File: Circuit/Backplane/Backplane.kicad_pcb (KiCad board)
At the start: 2 copper layers, 90.2 x 288.5 mm, 86 parts, among them CON1 peripheral_bridge, CON2 power_distributor, J1 USB_OTG, J2 power_source_mode, J3 general_power_source, J4 pneumatic, J5 pressure_sensor, J6 RS232_DVL, P1 imaging_sonar, P2 DVL, P3 computer1, P4 computer2, P5 ethernet_switch, P6 general, Q1 BC817-40, U1 LM1117-3.3, U2 TUSB4041I, U3 TLV73311PDBVT, Y1 24MHz

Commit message: FixVpcieWire
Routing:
- net VPCIE: track 224.6 -> 277.8 mm, vias 10 -> 11
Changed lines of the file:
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@@
   (general
     (links 258)
-    (no_connects 67)
-    (area 54.888001 -28.941011 180.062 277.020001)
+    (no_connects 2)
+    (area 76.124999 -26.745001 166.445001 261.949001)
     (thickness 1.6)
-    (drawings 32)
-    (tracks 1596)
+    (drawings 34)
+    (tracks 1606)
     (zones 0)
     (modules 86)
@@
   )
   (setup
-    (last_trace_width 0.254)
+    (last_trace_width 0.3048)
     (user_trace_width 0.2794)
     (user_trace_width 0.3048)
@@
     )
   )
+  (gr_line (start 134.62 160.02) (end 134.62 -7.62) (layer F.SilkS) (width 0.2))
+  (gr_line (start 91.44 119.888) (end 91.44 260.096) (layer F.SilkS) (width 0.2))
   (dimension 139.7 (width 0.3) (layer Eco1.User)
     (gr_text "139.700 mm" (at 124.126 62.268443 270) (layer Eco1.User)
@@
     (arrow2b (pts (xy 85.09 -25.4) (xy 85.676421 -24.273496)))
   )
-  (gr_text DSP (at 82.55 198.12 90) (layer Eco2.User)
+  (gr_text DSP (at 85.598 177.546 90) (layer Eco2.User)
     (effects (font (size 1.5 1.5) (thickness 0.3)))
   )
@@
     (arrow2b (pts (xy 91.44 119.634) (xy 90.853579 118.507496)))
   )
+  (segment (start 164.592 71.48373) (end 164.592 57.8612) (width 0.3048) (layer B.Cu) (net 1))
+  (segment (start 164.592 57.8612) (end 160.782 54.0512) (width 0.3048) (layer B.Cu) (net 1))
+  (segment (start 157.988 100.838) (end 159.283399 99.542601) (width 0.3048) (layer B.Cu) (net 1))
+  (segment (start 159.283399 99.542601) (end 159.283399 76.792331) (width 0.3048) (layer B.Cu) (net 1))
+  (segment (start 159.283399 76.792331) (end 164.592 71.48373) (width 0.3048) (layer B.Cu) (net 1))
+  (segment (start 159.512 102.108) (end 161.798 102.108) (width 0.3048) (layer F.Cu) (net 1))
+  (segment (start 157.988 102.108) (end 159.512 102.108) (width 0.3048) (layer F.Cu) (net 1))
+  (segment (start 159.512 102.108) (end 159.258 102.108) (width 0.3048) (layer F.Cu) (net 1))
+  (segment (start 159.258 102.108) (end 157.988 100.838) (width 0.3048) (layer F.Cu) (net 1))
+  (via (at 157.988 100.838) (size 1.10236) (drill 0.6096) (layers F.Cu B.Cu) (net 1))
   (segment (start 156.21 103.886) (end 157.988 102.108) (width 0.3048) (layer F.Cu) (net 1))
-  (segment (start 157.988 102.108) (end 161.798 102.108) (width 0.3048) (layer F.Cu) (net 1))
   (segment (start 149.352 108.204) (end 153.67 103.886) (width 0.3048) (layer B.Cu) (net 1))
   (segment (start 153.67 103.886) (end 156.21 103.886) (width 0.3048) (layer B.Cu) (net 1))
@@
   (segment (start 156.445799 -21.192201) (end 157.226 -20.412) (width 0.254) (layer F.Cu) (net 140))
   (segment (start 157.226 -20.412) (end 157.226 -19.558) (width 0.254) (layer F.Cu) (net 140))
+  (segment (start 143.885919 79.502) (end 143.885919 42.804081) (width 0.2794) (layer F.Cu) (net 141))
+  (segment (start 144.18309 83.096347) (end 144.18309 79.799171) (width 0.2794) (layer F.Cu) (net 141))
+  (segment (start 144.18309 79.799171) (end 143.885919 79.502) (width 0.2794) (layer F.Cu) (net 141))
   (segment (start 133.604 88.138) (end 137.24891 84.49309) (width 0.2794) (layer F.Cu) (net 141))
-  (segment (start 143.885919 82.799176) (end 143.885919 42.804081) (width 0.2794) (layer F.Cu) (net 141))
   (segment (start 137.24891 84.49309) (end 142.786347 84.49309) (width 0.2794) (layer F.Cu) (net 141))
   (segment (start 142.786347 84.49309) (end 144.18309 83.096347) (width 0.2794) (layer F.Cu) (net 141))
-  (segment (start 144.18309 83.096347) (end 143.885919 82.799176) (width 0.2794) (layer F.Cu) (net 141))
   (segment (start 133.858 32.776162) (end 133.858 -17.8126) (width 0.2794) (layer F.Cu) (net 141))
   (segment (start 143.885919 42.804081) (end 133.858 32.776162) (width 0.2794) (layer F.Cu) (net 141))

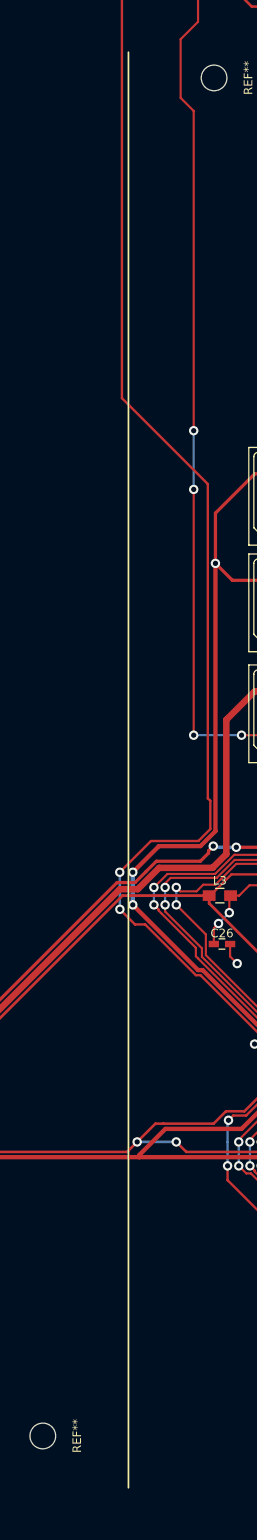
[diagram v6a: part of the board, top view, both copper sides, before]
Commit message: AddF.SilkSLine
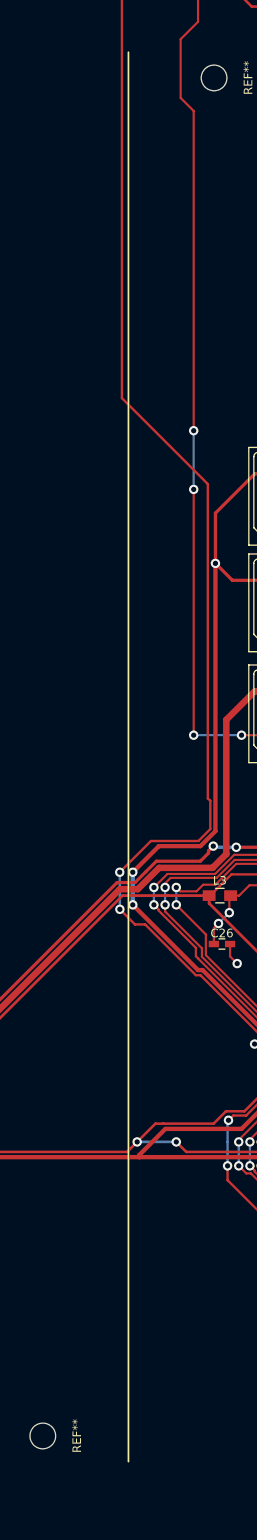
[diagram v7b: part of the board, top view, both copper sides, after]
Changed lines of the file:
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@@
     )
   )
-  (gr_line (start 134.62 160.02) (end 134.62 -7.62) (layer F.SilkS) (width 0.2))
+  (gr_line (start 134.62 -7.62) (end 134.62 156.972) (layer F.SilkS) (width 0.2))
   (gr_line (start 91.44 119.888) (end 91.44 260.096) (layer F.SilkS) (width 0.2))
   (dimension 139.7 (width 0.3) (layer Eco1.User)

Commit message: read new netlist and edit bug
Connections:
- D8 pad 1: +5V -> Net-(D8-Pad1)
- D8 pad 2: Net-(D8-Pad2) -> +5V
- R21 pad 1: Net-(D8-Pad2) -> Net-(D8-Pad1)
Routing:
- net +5V: track 398.4 -> 417.3 mm, vias 18 -> 19
- net +12V: track 444.6 -> 453.9 mm
- net Net-(C26-Pad1): track 22.9 -> 30.4 mm
- net Net-(D8-Pad2): track 6.63 -> 0.00 mm
- net Net-(D8-Pad1): track 0.00 -> 5.87 mm
- net GND: track 26.6 -> 29.7 mm
- net +1V1: track 286.8 -> 284.0 mm
- net Net-(CON1-PadB6): track 136.2 -> 138.6 mm
- net Net-(J1-Pad3): track 90.7 -> 89.3 mm
- net Net-(J1-Pad2): track 90.7 -> 89.3 mm
- net VPCIE: track 277.8 -> 276.4 mm
- net Net-(CON1-PadA7): track 166.9 -> 165.8 mm
- net Net-(CON1-PadA6): track 166.0 -> 165.0 mm
- net GNDA: track 190.9 -> 190.1 mm
- net VBUS: track 415.4 -> 414.6 mm
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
